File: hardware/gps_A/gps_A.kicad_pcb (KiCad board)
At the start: 2 copper layers, 119 x 92 mm, 90 parts, among them J1 RJ45, J10 KH-BNC50-3511, J4 USB_C_Receptacle, Q1 2N7002, Q10 2N7002, Q9 2N7002, U10 STM32F405RGTx, U11 AMS1117-3.3, U13 M24C02-RMN, U14 CH340C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

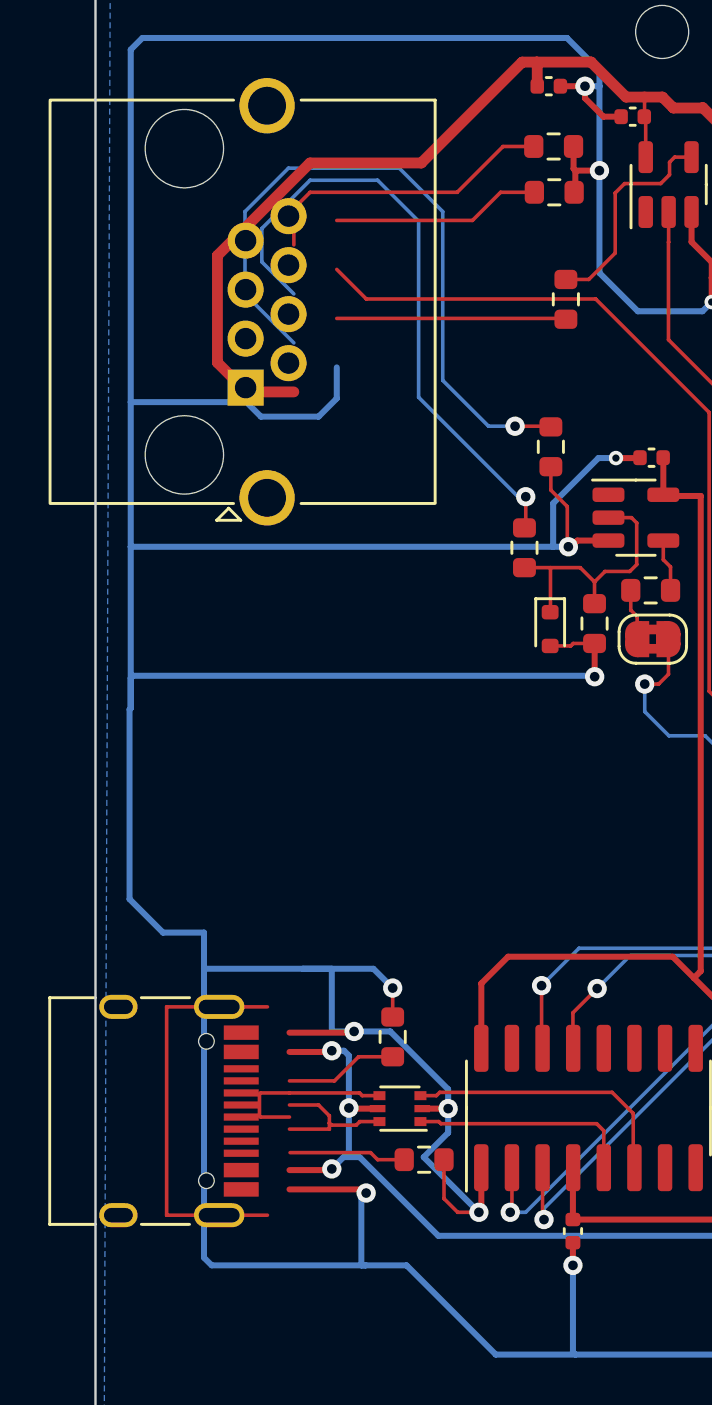
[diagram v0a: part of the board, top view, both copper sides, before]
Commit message: move RJ45 on gps
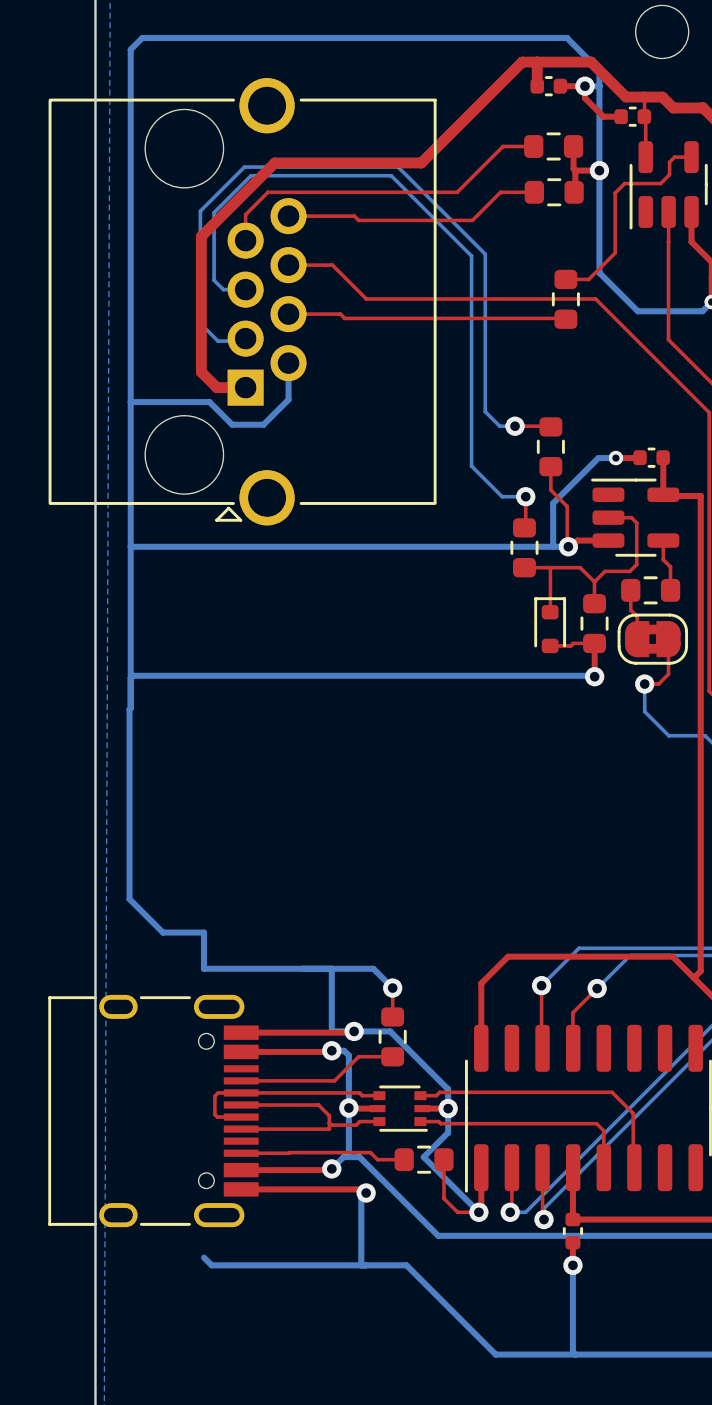
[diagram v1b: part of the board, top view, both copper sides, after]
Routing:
- net unconnected-(J4-SHIELD-PadS1): track 17.0 -> 0.00 mm
- net GND: track 871.3 -> 861.8 mm
- net VBUS: track 33.7 -> 37.7 mm
- net Net-(J4-D+-PadA6): track 6.22 -> 10.2 mm
- net /GPS_TX1H: track 26.0 -> 29.7 mm
- net /GPS_EN: track 28.2 -> 30.4 mm
- net /GPS_TX2H: track 8.68 -> 10.8 mm
- net /GPS_RX1H: track 9.47 -> 11.5 mm
- net /GPS_EXT_PPS: track 104.9 -> 107.0 mm
- net Net-(J4-CC2): track 4.85 -> 6.89 mm
- net Net-(J4-CC1): track 4.69 -> 6.69 mm
- net /GPS_RX2H: track 12.5 -> 14.2 mm
- net Net-(J4-D--PadA7): track 7.21 -> 8.82 mm

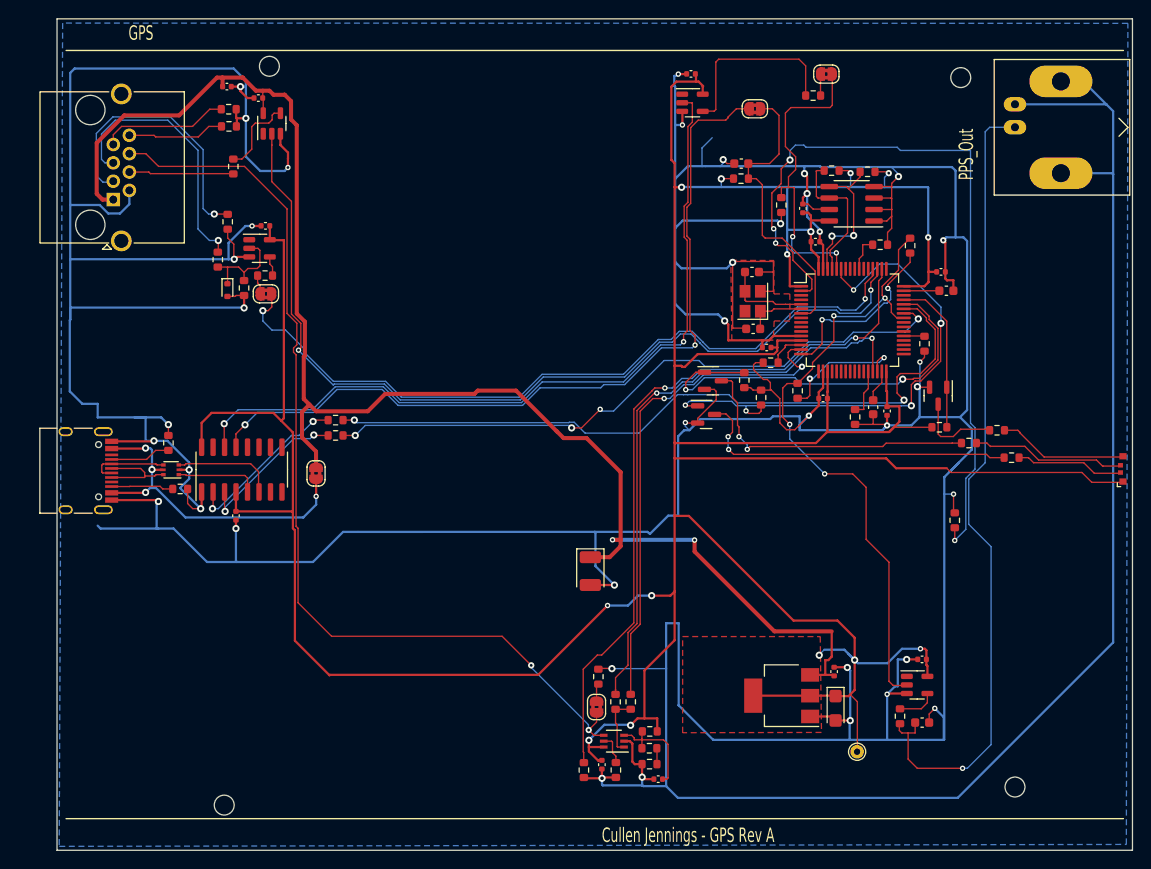
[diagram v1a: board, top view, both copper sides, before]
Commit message: start generation of GPS rev A.1 production files
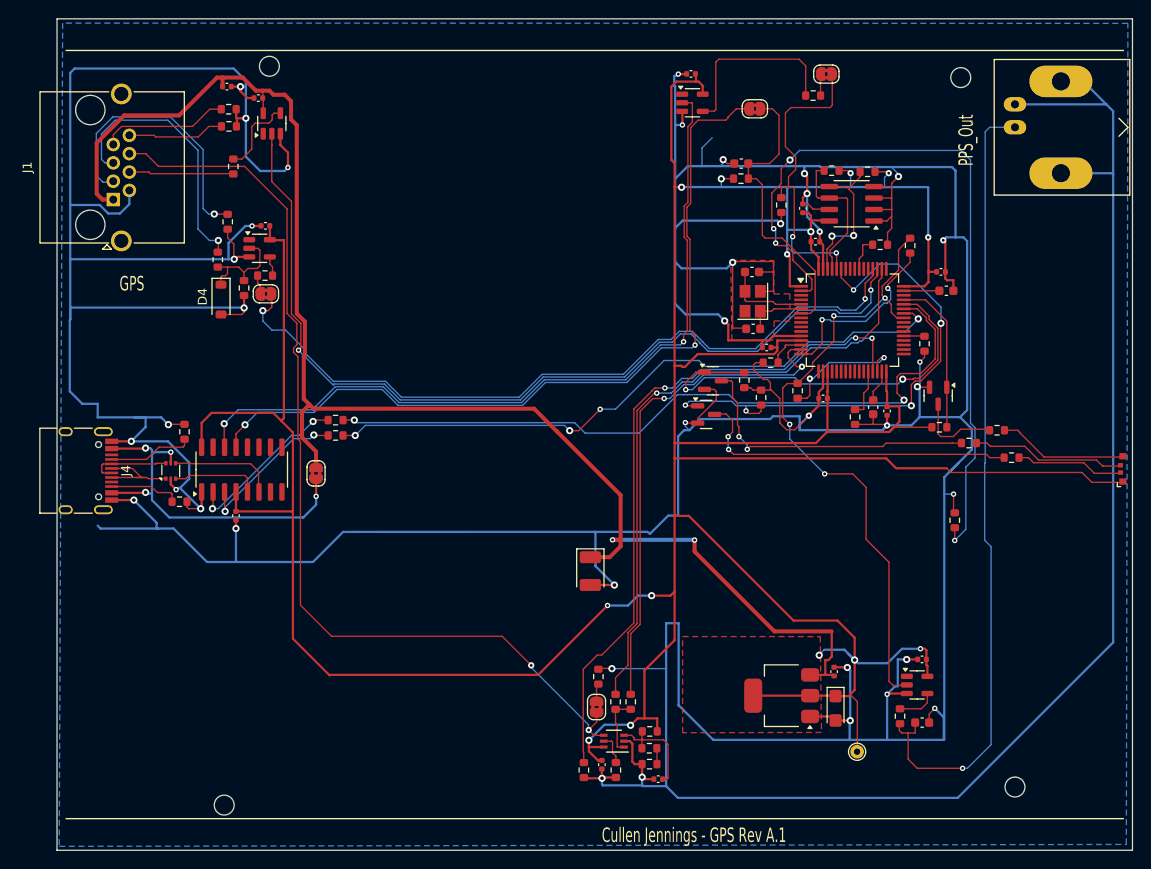
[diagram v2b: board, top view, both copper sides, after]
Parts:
- D4: value SDM20U30-7 -> B5819W SL; footprint Diode_SMD:D_SOD-523 -> Diode_SMD:D_SOD-123
- J1: footprint Connector_RJ:RJ45_Amphenol_RJHSE5380 -> blinky_footprints:RJ45_Amphenol_RJHSE5380
- J4: footprint Connector_USB:USB_C_Receptacle_HRO_TYPE-C-31-M-12 -> blinky_footprints:USB_C_Receptacle_HRO_TYPE-C-31-M-12
- moved R38 2.17 mm to (109.1, 83.7)
- moved R37 1.42 mm to (108.6, 91.4)
- moved D4 1.27 mm to (113.1, 69.1)
- moved U15 0.13 mm to (107.6, 88.0), turned to 90 degrees
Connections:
- U15 pad 1: Net-(U14-UD+) -> Net-(J4-D+-PadA6)
- U15 pad 3: Net-(U14-UD-) -> Net-(U14-UD+)
- U15 pad 4: Net-(J4-D--PadA7) -> Net-(U14-UD-)
- U15 pad 6: Net-(J4-D+-PadA6) -> Net-(J4-D--PadA7)
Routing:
- net +5V: track 168.7 -> 165.3 mm
- net VBUS: track 37.7 -> 40.4 mm
- net Net-(J4-CC1): track 6.69 -> 9.40 mm
- net /BTN1: track 85.9 -> 84.2 mm
- net Net-(J10-In): track 90.4 -> 88.9 mm
- net Net-(J4-CC2): track 6.89 -> 7.88 mm
- net Net-(D4-K): track 10.9 -> 11.5 mm
- net GND: track 861.8 -> 861.2 mm
- net Net-(J4-D+-PadA6): track 10.2 -> 10.7 mm
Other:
- board text added: "Cullen Jennings - GPS Rev A.1"
- board text removed: "Cullen Jennings - GPS Rev A"

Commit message: version of GPS Rev A.1  submitted to JLCPCB
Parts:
- moved U15 0.17 mm to (107.4, 88.0), turned to 180 degrees
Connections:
- U15 pad 1: Net-(J4-D+-PadA6) -> Net-(U14-UD+)
- U15 pad 3: Net-(U14-UD+) -> Net-(U14-UD-)
- U15 pad 4: Net-(U14-UD-) -> Net-(J4-D--PadA7)
- U15 pad 6: Net-(J4-D--PadA7) -> Net-(J4-D+-PadA6)
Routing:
- net VBUS: track 40.4 -> 38.9 mm

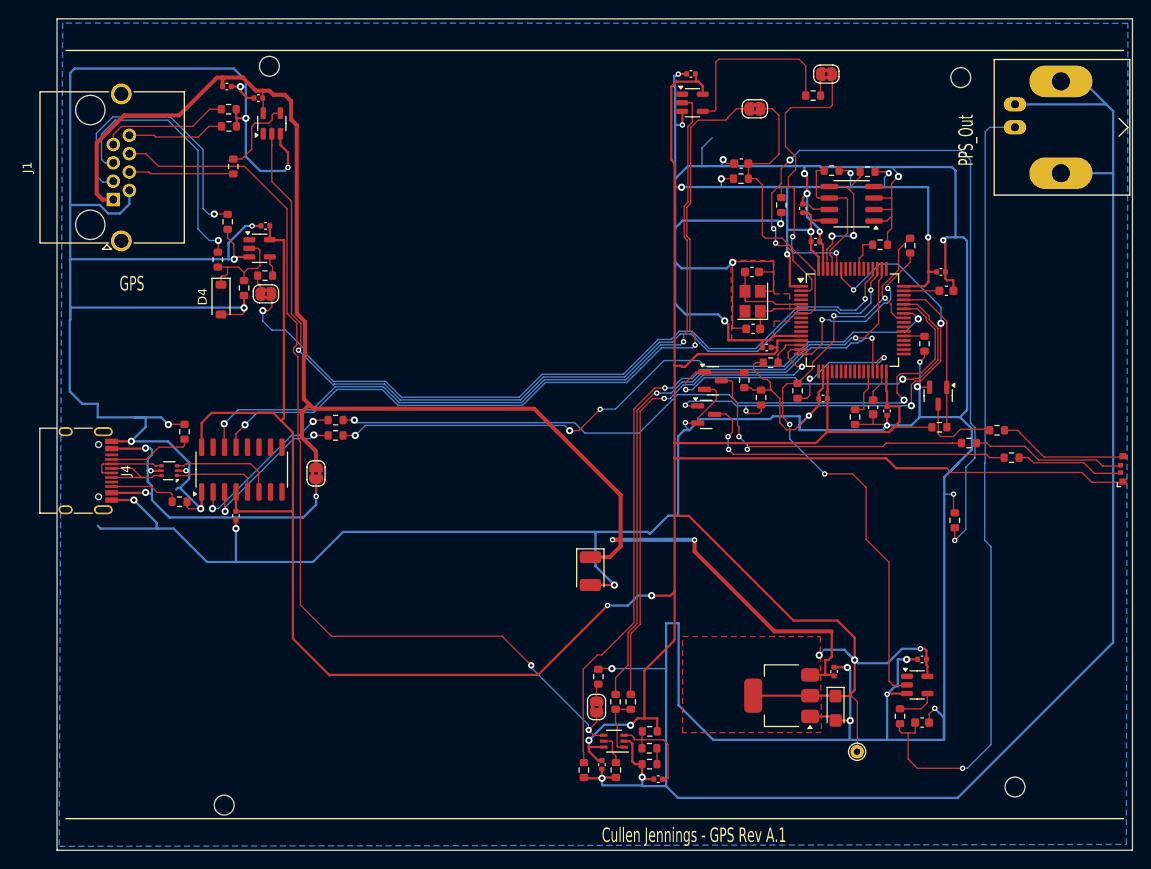
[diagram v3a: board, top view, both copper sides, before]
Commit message: remove tal caps on GPS, clean up schamatic
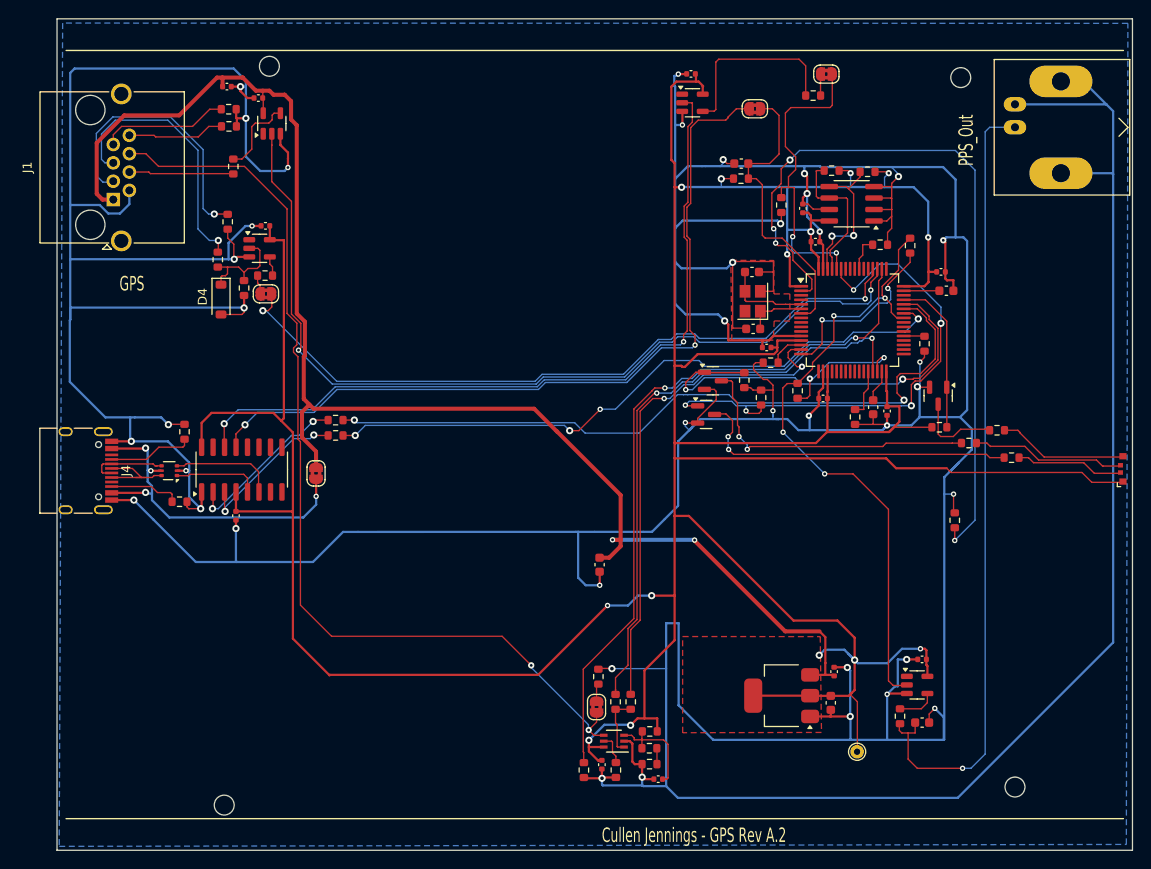
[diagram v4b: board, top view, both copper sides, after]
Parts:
- removed C41: 10u, Capacitor_Tantalum_SMD:CP_EIA-3216-18_Kemet-A
- added C2: 10u, Capacitor_SMD:C_0603_1608Metric, F.Cu at (180.6, 113.7)
- C42: value 33u -> 10u; footprint Capacitor_Tantalum_SMD:CP_EIA-3528-21_Kemet-B -> Capacitor_SMD:C_0603_1608Metric
- moved C42 1.24 mm to (155.0, 98.4)
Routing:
- net GND: track 861.1 -> 839.9 mm, vias 38 -> 39
- net /GPS_TX1: track 84.3 -> 80.7 mm
- net +5V: track 165.3 -> 162.0 mm
- net /GPS_RX1: track 101.5 -> 98.7 mm
- net /USB_DTR: track 89.8 -> 88.3 mm
- net /USB_RTS: track 86.9 -> 85.4 mm
- net +3.3V: track 460.8 -> 459.9 mm
- net VBUS: track 38.9 -> 38.2 mm
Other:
- board text added: "Cullen Jennings - GPS Rev A.2"
- board text removed: "Cullen Jennings - GPS Rev A.1"

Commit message: order GPS A.2
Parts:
- U8: footprint blinky_footprints:SC70_DCK_TEX -> Package_TO_SOT_SMD:SOT-363_SC-70-6

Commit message: updates for GPS Rev A.3
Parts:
- removed R28: 47K, Resistor_SMD:R_0603_1608Metric
- removed R32: 4K7, Resistor_SMD:R_0603_1608Metric
- added J6: Conn_01x03, Connector_JST:JST_PH_S3B-PH-SM4-TB_1x03-1MP_P2.00mm_Horizontal, F.Cu at (204.6, 72.5)
- Y2: value 16MHz -> 16MHz
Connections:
- net AUX_GPS_PPS renamed /AUX_GPS_PPS
- net GPS_PPS renamed /GPS_PPS
- net PPS_OUT renamed /PPS_OUT
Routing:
- net /SWDCLK: track 0.00 -> 26.7 mm
- net /SWDIO: track 0.00 -> 16.8 mm
- net GND: track 839.9 -> 848.2 mm, vias 39 -> 40

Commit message: update all harware revs
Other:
- board text added: "Cullen Jennings - GPS Rev A.3 2025"
- board text removed: "Cullen Jennings - GPS Rev A.2"
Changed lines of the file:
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@@
 	(title_block
 		(title "GPS")
-		(date "2024-06-16")
-		(rev "A.2")
+		(date "2025-06-15")
+		(rev "A.3")
 		(company "Cullen Jennings")
 	)
@@
 		(layer "Edge.Cuts")
 	)
-	(gr_text "Cullen Jennings - GPS Rev A.2\n"
+	(gr_text "Cullen Jennings - GPS Rev A.3  2025\n"
 		(at 155.280231 129.271842 0)
 		(layer "F.SilkS")
